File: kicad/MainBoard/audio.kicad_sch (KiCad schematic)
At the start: 52 parts, among them J18 AudioJack3_SwitchTR, Q14 AO3401A, Q15 AO3401A, U10 MCP4651, U11 LM324, U12 SN74LVC1G3157DCKR, U18 SN74LVC1G3157DCKR, U25 USBLC6-2P6

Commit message: Add PCB v2.3 kicad project files + gerbers
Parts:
- removed C44: 10uF, Capacitor_SMD:C_0603_1608Metric_Pad1.08x0.95mm_HandSolder, symbol Device:C_Polarized_Small
- added C44: 1uF, Capacitor_SMD:C_0603_1608Metric_Pad1.08x0.95mm_HandSolder, symbol Device:C_Small
- added U16: HT7533-1, Package_TO_SOT_SMD:SOT-89-3, symbol Regulator_Linear:HT75xx-1-SOT89
- C32, C36: value 10uF -> 1uF; LCSC C19702 -> C15849
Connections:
- net 5v: now also C44.2, U16.2 (VIN)
- net AUDIO_IN_L: now also C32.1; no longer C32.2
- net AUDIO_IN_R: now also C36.1; no longer C36.2
- net GND: now also C44.1, U16.1 (GND)
- net at R123.2, U25.3 (I/O2): now also C32.2; no longer C32.1
- net at R120.2, U25.1 (I/O1): now also C36.2; no longer C36.1
- net 3v3 renamed 3v3_LDO
- net 3v3_LDO: now also U16.3 (VOUT)

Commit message: v2.5 schematic + PCB changes
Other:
- company: (none) -> CrashOverride85
- title: (none) -> ZC95 MKII
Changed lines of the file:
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@@
 (kicad_sch (version 20211123) (generator eeschema)
   (paper "A4")
+  (title_block
+    (title "ZC95 MKII")
+    (rev "2.5")
+    (company "CrashOverride85")
+  )
   (junction (at 99.06 97.155) (diameter 0) (color 0 0 0 0)
   )

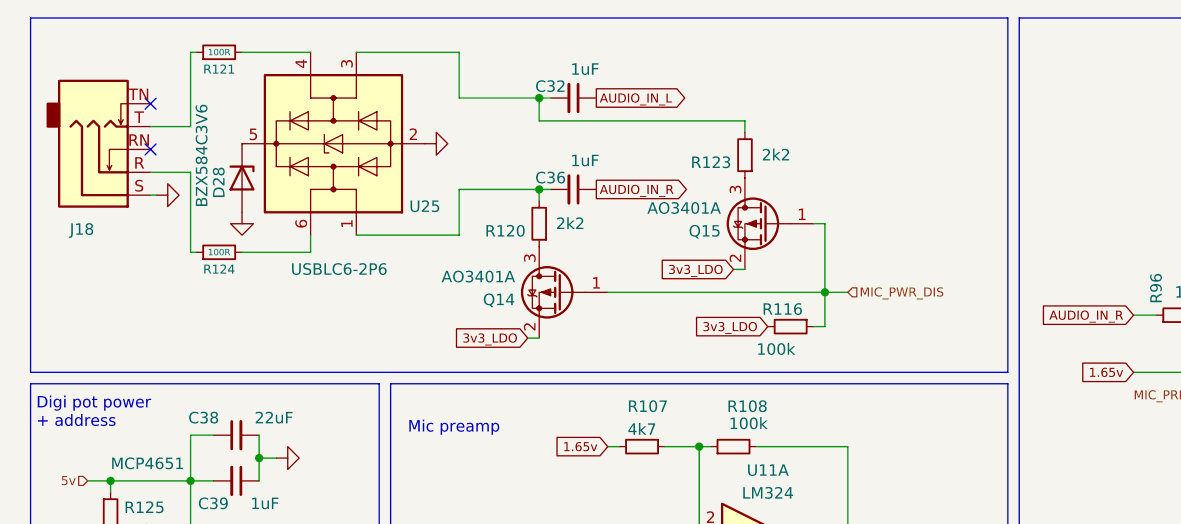
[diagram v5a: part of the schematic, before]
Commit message: v2.6 schematic + pcb changes
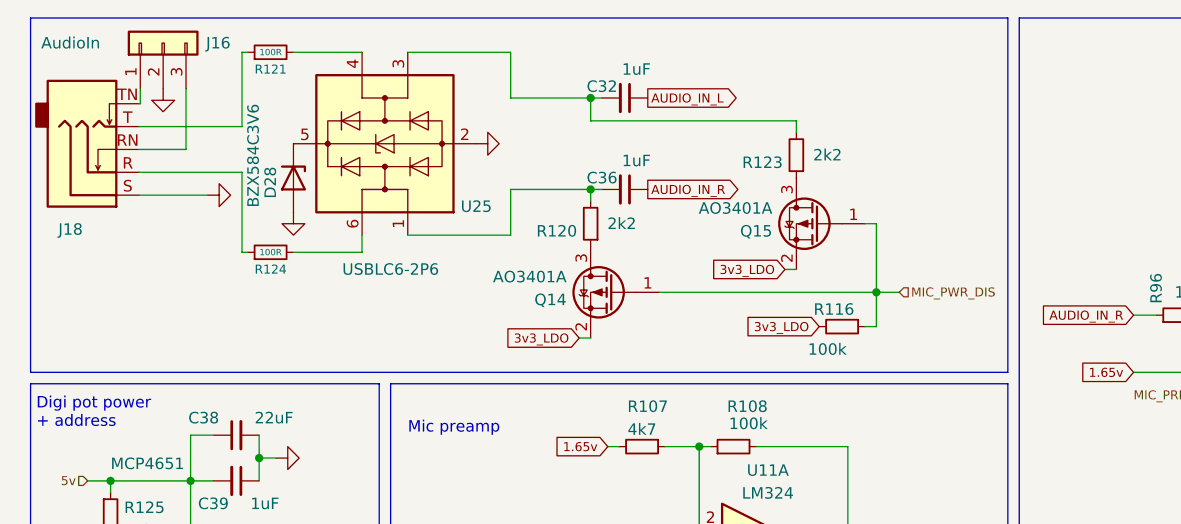
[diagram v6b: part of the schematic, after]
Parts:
- added J16: AudioIn, Connector_PinSocket_2.54mm:PinSocket_1x03_P2.54mm_Vertical, symbol Connector_Generic:Conn_01x03
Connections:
- net GND: now also J16.2 (Pin_2)
- net at J18.RN: now also J16.3 (Pin_3)
- net at J18.TN: now also J16.1 (Pin_1)
- no-connect marks 4 -> 2
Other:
- moved on the sheet: C32, C36, D28, J18, Q14, Q15, R116, R120, R121, R123, R124, U25
